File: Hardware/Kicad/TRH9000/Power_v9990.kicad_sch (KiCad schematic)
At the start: 21 parts, among them U1 V9990, U2 KM428C256, U3 KM428C256, U4 74VHC138, U6 LMH1980, U7 T.I_SN74AHCT32D

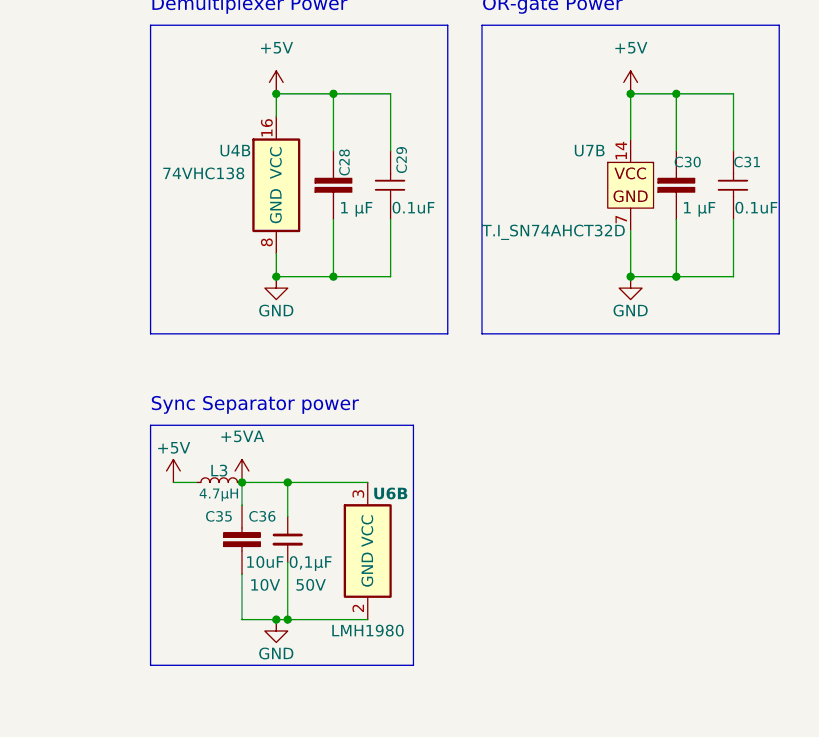
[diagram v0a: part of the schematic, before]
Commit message: Multiple updates. Routing. Almost finished routing for the VDP. Moved back the footprint for the 14mhz oscillator to THT as it is easier to find outside US/Europe and I have a bunch laying around here. Organized all components into the PCB. Removed the holed in the cartridge so I can better measure them in the standard MSX cartridge. Changed the RGB connector footprint to a shorter version so we can fit it in the standard size cartridge. Fixed multiple footprints to 0805 as we will be standardizing in that size.
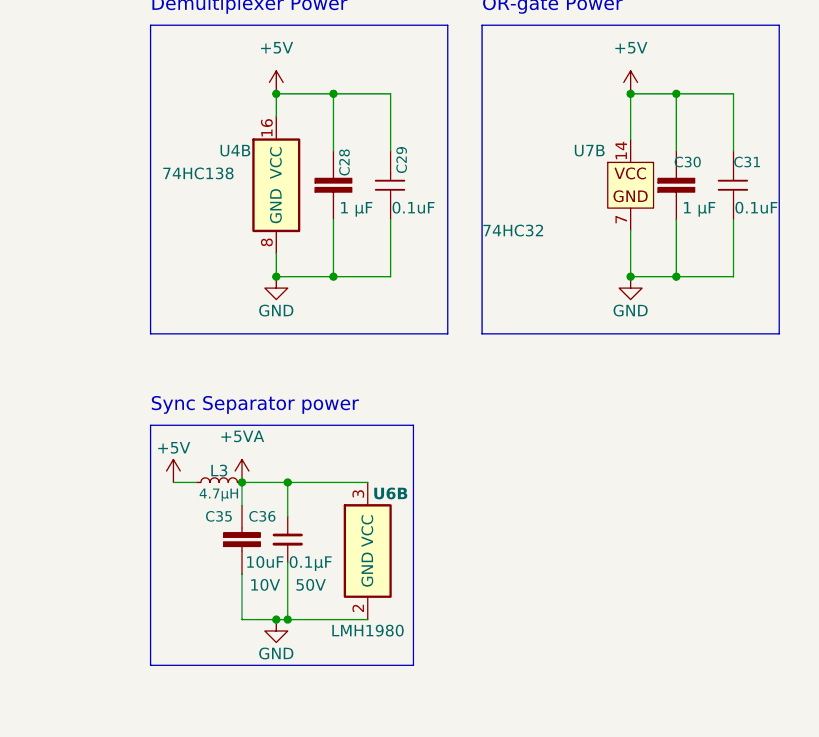
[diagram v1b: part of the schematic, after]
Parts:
- C28, C30: value C_CL21B105KBFNNNF -> 1 µF; footprint Capacitor_SMD:C_0805_2012Metric_Pad1.18x1.45mm_HandSolder -> Capacitor_SMD:C_0805_2012Metric
- C29: value C_CC0805JPX7R9BB104 -> 0.1uF; MPN CC0805JPX7R9BB104 -> (none); Manufacturer Yageo -> (none); Mounting type SMD -> (none); Mouser datasheet https://www.mouser.se/datasheet/2/427/vjcommercialseries-17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 -> (none); Price €0,14 -> (none); Status Active -> (none); Temperature Coefficient  X7R -> (none); Voltage rating 50V -> (none)
- C3: value C_GRM21BR61A476ME15K -> 47uF
- C31: value C_CC0805JPX7R9BB104 -> 0.1uF; MPN CC0805JPX7R9BB104 -> (none); Manufacturer Yageo -> (none); Mouser datasheet https://www.mouser.se/datasheet/2/427/vjcommercialseries-17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 -> (none)
- C35: value C_GRM21BR71A106KA73K -> 10uF
- C36: value C_CL10B104KB8NNNL -> 0.1µF; footprint Capacitor_SMD:C_0603_1608Metric_Pad1.08x0.95mm_HandSolder -> Capacitor_SMD:C_0805_2012Metric; Capacitance  0,1µF -> 0.1µF
- C5, C7: value C_CC0805JPX7R9BB104 -> 0.1uF
- L3: value L_MLZ2012M4R7HT000 -> 4.7µH
- U4: value 74VHC138 -> 74HC138; MPN 74VHC138FT -> 74HC138
- U7: value T.I_SN74AHCT32D -> 74HC32; footprint trh9000:Texas_R-PDSO-G14_3.6x4.4mm -> Package_SO:SO-14_3.9x8.65mm_P1.27mm; MPN SN74AHCT32DGVR -> 74HC32
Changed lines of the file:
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@@
       (effects (font (size 1.143 1.143)) (justify left))
     )
-    (property "Value" "C_CC0805JPX7R9BB104" (id 1) (at 193.04 53.34 0)
+    (property "Value" "0.1uF" (id 1) (at 193.04 53.34 0)
       (effects (font (size 1.143 1.143)) (justify left bottom) hide)
     )
@@
       (effects (font (size 1.143 1.143)))
     )
-    (property "Value" "C_CL21B105KBFNNNF" (id 1) (at 62.484 46.609 0)
+    (property "Value" "1 µF" (id 1) (at 62.484 46.609 0)
       (effects (font (size 1.143 1.143)) (justify left bottom) hide)
     )
-    (property "Footprint" "Capacitor_SMD:C_0805_2012Metric_Pad1.18x1.45mm_HandSolder" (id 2) (at 60.96 52.07 0)
+    (property "Footprint" "Capacitor_SMD:C_0805_2012Metric" (id 2) (at 60.96 52.07 0)
       (effects (font (size 0.508 0.508)) hide)
     )
@@
       (effects (font (size 1.143 1.143)) (justify left))
     )
-    (property "Value" "C_CL10B104KB8NNNL" (id 1) (at 55.626 84.582 0)
+    (property "Value" " 0.1µF" (id 1) (at 55.626 84.582 0)
       (effects (font (size 1.27 1.27)) (justify left) hide)
     )
-    (property "Footprint" "Capacitor_SMD:C_0603_1608Metric_Pad1.08x0.95mm_HandSolder" (id 2) (at 2.54 91.44 0)
+    (property "Footprint" "Capacitor_SMD:C_0805_2012Metric" (id 2) (at 2.54 91.44 0)
       (effects (font (size 1.27 1.27)) hide)
     )
@@
       (effects (font (size 2.54 2.54)) hide)
     )
-    (property "Capacitance " " 0,1µF" (id 7) (at 58.42 85.09 0))
+    (property "Capacitance " " 0.1µF" (id 7) (at 58.42 85.09 0))
     (property "Tolerance" " ±10% " (id 8) (at 29.21 72.39 0)
       (effects (font (size 2.54 2.54)) hide)
@@
       (effects (font (size 1.27 1.27)) (justify left))
     )
-    (property "Value" "74VHC138" (id 1) (at 41.91 41.91 0)
+    (property "Value" "74HC138" (id 1) (at 41.91 41.91 0)
       (effects (font (size 1.27 1.27)) (justify left))
     )
@@
       (effects (font (size 1.27 1.27)) hide)
     )
-    (property "MPN" "74VHC138FT" (id 4) (at 80.01 45.72 0)
+    (property "MPN" "74HC138" (id 4) (at 80.01 45.72 0)
       (effects (font (size 1.27 1.27)) hide)
     )
@@
       (effects (font (size 1.143 1.143)) (justify left))
     )
-    (property "Value" "C_CC0805JPX7R9BB104" (id 1) (at 214.63 53.34 0)
+    (property "Value" "0.1uF" (id 1) (at 214.63 53.34 0)
       (effects (font (size 1.143 1.143)) (justify left bottom) hide)
     )
@@
     (in_bom yes) (on_board yes)
     (property "Reference" "L3" (id 0) (at 48.26 74.93 90))
-    (property "Value" "L_MLZ2012M4R7HT000" (id 1) (at 49.276 75.438 0)
+    (property "Value" "4.7µH" (id 1) (at 49.276 75.438 0)
       (effects (font (size 1.27 1.27)) (justify left) hide)
     )
@@
       (effects (font (size 1.143 1.143)) (justify left))
     )
-    (property "Value" "C_GRM21BR61A476ME15K" (id 1) (at 161.29 73.66 0)
+    (property "Value" "47uF" (id 1) (at 161.29 73.66 0)
       (effects (font (size 1.143 1.143)) (justify left) hide)
     )
@@
       (effects (font (size 1.143 1.143)) (justify left))
     )
-    (property "Value" "C_CC0805JPX7R9BB104" (id 1) (at 72.39 49.53 0)
+    (property "Value" "0.1uF" (id 1) (at 72.39 49.53 0)
       (effects (font (size 1.143 1.143)) (justify left bottom) hide)
     )
@@
       (effects (font (size 0.508 0.508)) hide)
     )
-    (property "Datasheet" "https://www.yageo.com/upload/media/product/productsearch/datasheet/mlcc/UPY-GPHC_X7R_6.3V-to-50V_18.pdf" (id 3) (at 67.31 44.45 0)
-      (effects (font (size 1.27 1.27)) hide)
-    )
-    (property "Manufacturer" "Yageo" (id 4) (at 76.2 39.37 0)
-      (effects (font (size 1.27 1.27)) hide)
-    )
-    (property "MPN" "CC0805JPX7R9BB104" (id 5) (at 69.85 44.4499 0)
-      (effects (font (size 1.27 1.27)) (justify left) hide)
-    )
-    (property "Mouser datasheet" "https://www.mouser.se/datasheet/2/427/vjcommercialseries-1764145.pdf" (id 6) (at 109.22 41.91 0)
+    (property "Datasheet" "" (id 3) (at 67.31 44.45 0)
       (effects (font (size 1.27 1.27)) hide)
     )
     (property "Capacitance" "0.1uF" (id 7) (at 69.85 45.72 0))
-    (property "Voltage rating" "50V" (id 8) (at 74.93 46.99 0)
-      (effects (font (size 1.27 1.27)) hide)
-    )
-    (property "Temperature Coefficient " "X7R" (id 9) (at 74.93 52.07 0)
-      (effects (font (size 1.27 1.27)) hide)
-    )
-    (property "Mounting type" "SMD" (id 10) (at 76.2 59.69 0)
-      (effects (font (size 1.27 1.27)) hide)
-    )
-    (property "Status" "Active" (id 11) (at 76.2 54.61 0)
-      (effects (font (size 1.27 1.27)) hide)
-    )
-    (property "Price" "€0,14" (id 12) (at 76.2 57.15 0)
-      (effects (font (size 1.27 1.27)) hide)
-    )
     (pin "1")
     (pin "2")
@@
       (effects (font (size 1.143 1.143)))
     )
-    (property "Value" "C_CL21B105KBFNNNF" (id 1) (at 100.584 46.609 0)
+    (property "Value" "1 µF" (id 1) (at 100.584 46.609 0)
       (effects (font (size 1.143 1.143)) (justify left bottom) hide)
     )
-    (property "Footprint" "Capacitor_SMD:C_0805_2012Metric_Pad1.18x1.45mm_HandSolder" (id 2) (at 99.06 52.07 0)
+    (property "Footprint" "Capacitor_SMD:C_0805_2012Metric" (id 2) (at 99.06 52.07 0)
       (effects (font (size 0.508 0.508)) hide)
     )
@@
       (effects (font (size 1.143 1.143)) (justify left))
     )
-    (property "Value" "C_CC0805JPX7R9BB104" (id 1) (at 110.49 49.53 0)
+    (property "Value" "0.1uF" (id 1) (at 110.49 49.53 0)
       (effects (font (size 1.143 1.143)) (justify left bottom) hide)
     )
@@
     )
     (property "Datasheet" "https://www.yageo.com/upload/media/product/productsearch/datasheet/mlcc/UPY-GPHC_X7R_6.3V-to-50V_18.pdf" (id 3) (at 105.41 44.45 0)
-      (effects (font (size 1.27 1.27)) hide)
-    )
-    (property "Manufacturer" "Yageo" (id 4) (at 114.3 39.37 0)
-      (effects (font (size 1.27 1.27)) hide)
-    )
-    (property "MPN" "CC0805JPX7R9BB104" (id 5) (at 107.95 44.4499 0)
-      (effects (font (size 1.27 1.27)) (justify left) hide)
-    )
-    (property "Mouser datasheet" "https://www.mouser.se/datasheet/2/427/vjcommercialseries-1764145.pdf" (id 6) (at 147.32 41.91 0)
       (effects (font (size 1.27 1.27)) hide)
     )
@@
       (effects (font (size 1.143 1.143)))
     )
-    (property "Value" "C_GRM21BR71A106KA73K" (id 1) (at 52.07 85.09 0)
+    (property "Value" "10uF" (id 1) (at 52.07 85.09 0)
       (effects (font (size 1.143 1.143)) (justify left bottom) hide)
     )
@@
       (effects (font (size 1.27 1.27)) (justify left))
     )
-    (property "Value" "T.I_SN74AHCT32D" (id 1) (at 77.47 48.26 0)
-      (effects (font (size 1.27 1.27)) (justify left))
-    )
-    (property "Footprint" "trh9000:Texas_R-PDSO-G14_3.6x4.4mm" (id 2) (at 106.68 40.64 0)
+    (property "Value" "74HC32" (id 1) (at 77.47 48.26 0)
+      (effects (font (size 1.27 1.27)) (justify left))
+    )
+    (property "Footprint" "Package_SO:SO-14_3.9x8.65mm_P1.27mm" (id 2) (at 106.68 40.64 0)
       (effects (font (size 1.524 1.524)) (justify left) hide)
     )
@@
       (effects (font (size 1.524 1.524)) (justify left) hide)
     )
-    (property "MPN" "SN74AHCT32DGVR" (id 5) (at 106.68 33.02 0)
+    (property "MPN" "74HC32" (id 5) (at 106.68 33.02 0)
       (effects (font (size 1.524 1.524)) (justify left) hide)
     )

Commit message: Routing, readme, etc
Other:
- moved on the sheet: U1D
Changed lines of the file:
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@@
     (stroke (width 0) (type default) (color 0 0 0 0))
   )
-  (wire (pts (xy 125.73 48.26) (xy 128.27 48.26))
+  (wire (pts (xy 133.35 48.26) (xy 135.89 48.26))
     (stroke (width 0) (type default) (color 0 0 0 0))
   )
@@
     (stroke (width 0) (type default) (color 0 0 0 0))
   )
-  (wire (pts (xy 133.35 48.26) (xy 135.89 48.26))
+  (wire (pts (xy 140.97 48.26) (xy 143.51 48.26))
     (stroke (width 0) (type default) (color 0 0 0 0))
   )
@@
     (stroke (width 0) (type default) (color 0 0 0 0))
   )
+  (wire (pts (xy 140.97 33.02) (xy 143.51 33.02))
+    (stroke (width 0) (type default) (color 0 0 0 0))
+  )
+  (wire (pts (xy 157.48 68.58) (xy 171.45 68.58))
+    (stroke (width 0) (type default) (color 0 0 0 0))
+  )
+  (wire (pts (xy 170.18 39.37) (xy 167.64 39.37))
+    (stroke (width 0) (type default) (color 0 0 0 0))
+  )
+  (polyline (pts (xy 40.64 25.4) (xy 40.64 59.69))
+    (stroke (width 0) (type default) (color 0 0 0 0))
+  )
+  (polyline (pts (xy 115.57 25.4) (xy 115.57 90.17))
+    (stroke (width 0) (type default) (color 0 0 0 0))
+  )
+  (wire (pts (xy 105.41 33.02) (xy 99.06 33.02))
+    (stroke (width 0) (type default) (color 0 0 0 0))
+  )
   (wire (pts (xy 133.35 33.02) (xy 135.89 33.02))
-    (stroke (width 0) (type default) (color 0 0 0 0))
-  )
-  (wire (pts (xy 157.48 68.58) (xy 171.45 68.58))
-    (stroke (width 0) (type default) (color 0 0 0 0))
-  )
-  (wire (pts (xy 170.18 39.37) (xy 167.64 39.37))
-    (stroke (width 0) (type default) (color 0 0 0 0))
-  )
-  (polyline (pts (xy 40.64 25.4) (xy 40.64 59.69))
-    (stroke (width 0) (type default) (color 0 0 0 0))
-  )
-  (polyline (pts (xy 115.57 25.4) (xy 115.57 90.17))
-    (stroke (width 0) (type default) (color 0 0 0 0))
-  )
-  (wire (pts (xy 105.41 33.02) (xy 99.06 33.02))
-    (stroke (width 0) (type default) (color 0 0 0 0))
-  )
-  (wire (pts (xy 125.73 33.02) (xy 128.27 33.02))
     (stroke (width 0) (type default) (color 0 0 0 0))
   )
@@
     (pin "2")
   )
-  (symbol (lib_id "power:+5VA") (at 135.89 33.02 0) (unit 1)
-    (in_bom yes) (on_board yes)
-    (property "Reference" "#PWR0109" (id 0) (at 135.89 36.83 0)
-      (effects (font (size 1.27 1.27)) hide)
-    )
-    (property "Value" "+5VA" (id 1) (at 136.271 28.6258 0))
-    (property "Footprint" "" (id 2) (at 135.89 33.02 0)
-      (effects (font (size 1.27 1.27)) hide)
-    )
-    (property "Datasheet" "" (id 3) (at 135.89 33.02 0)
+  (symbol (lib_id "power:+5VA") (at 143.51 33.02 0) (unit 1)
+    (in_bom yes) (on_board yes)
+    (property "Reference" "#PWR0109" (id 0) (at 143.51 36.83 0)
+      (effects (font (size 1.27 1.27)) hide)
+    )
+    (property "Value" "+5VA" (id 1) (at 143.891 28.6258 0))
+    (property "Footprint" "" (id 2) (at 143.51 33.02 0)
+      (effects (font (size 1.27 1.27)) hide)
+    )
+    (property "Datasheet" "" (id 3) (at 143.51 33.02 0)
       (effects (font (size 1.27 1.27)) hide)
     )
@@
     (pin "1")
   )
-  (symbol (lib_id "power:GND") (at 125.73 48.26 0) (unit 1)
-    (in_bom yes) (on_board yes)
-    (property "Reference" "#PWR0123" (id 0) (at 125.73 54.61 0)
-      (effects (font (size 1.27 1.27)) hide)
-    )
-    (property "Value" "GND" (id 1) (at 125.857 52.6542 0))
-    (property "Footprint" "" (id 2) (at 125.73 48.26 0)
-      (effects (font (size 1.27 1.27)) hide)
-    )
-    (property "Datasheet" "" (id 3) (at 125.73 48.26 0)
+  (symbol (lib_id "power:GND") (at 133.35 48.26 0) (unit 1)
+    (in_bom yes) (on_board yes)
+    (property "Reference" "#PWR0123" (id 0) (at 133.35 54.61 0)
+      (effects (font (size 1.27 1.27)) hide)
+    )
+    (property "Value" "GND" (id 1) (at 133.477 52.6542 0))
+    (property "Footprint" "" (id 2) (at 133.35 48.26 0)
+      (effects (font (size 1.27 1.27)) hide)
+    )
+    (property "Datasheet" "" (id 3) (at 133.35 48.26 0)
       (effects (font (size 1.27 1.27)) hide)
     )
@@
     (pin "1")
   )
-  (symbol (lib_id "TRH9000:V9990") (at 130.81 40.64 0) (unit 4)
-    (in_bom yes) (on_board yes)
-    (property "Reference" "U1" (id 0) (at 121.92 36.83 0)
+  (symbol (lib_id "TRH9000:V9990") (at 138.43 40.64 0) (unit 4)
+    (in_bom yes) (on_board yes)
+    (property "Reference" "U1" (id 0) (at 129.54 36.83 0)
       (effects (font (size 1.27 1.27)) (justify left))
     )
-    (property "Value" "V9990" (id 1) (at 121.92 44.45 0)
+    (property "Value" "V9990" (id 1) (at 129.54 44.45 0)
       (effects (font (size 1.524 1.524)) (justify left))
     )
-    (property "Footprint" "trh9000:LQFP-128_28x28mm_P0.8mm" (id 2) (at 130.81 40.64 0)
+    (property "Footprint" "trh9000:LQFP-128_28x28mm_P0.8mm" (id 2) (at 138.43 40.64 0)
       (effects (font (size 1.524 1.524)) hide)
     )
-    (property "Datasheet" "https://www.msx.org/wiki/Yamaha_V9990" (id 3) (at 130.81 40.64 0)
+    (property "Datasheet" "https://www.msx.org/wiki/Yamaha_V9990" (id 3) (at 138.43 40.64 0)
       (effects (font (size 1.524 1.524)) hide)
     )
-    (property "Manufacturer" "Yamaha" (id 4) (at 67.31 -7.62 0)
+    (property "Manufacturer" "Yamaha" (id 4) (at 74.93 -7.62 0)
       (effects (font (size 1.524 1.524)) hide)
     )
-    (property "MPN" "V9990" (id 5) (at 67.31 0 0)
+    (property "MPN" "V9990" (id 5) (at 74.93 0 0)
       (effects (font (size 1.524 1.524)) hide)
     )
-    (property "Description" "Video Display Processor (VDP)" (id 6) (at 80.01 -5.08 0)
+    (property "Description" "Video Display Processor (VDP)" (id 6) (at 87.63 -5.08 0)
       (effects (font (size 1.524 1.524)) hide)
     )
@@
     (pin "96")
   )
-  (symbol (lib_id "power:GNDA") (at 135.89 48.26 0) (unit 1)
-    (in_bom yes) (on_board yes)
-    (property "Reference" "#PWR0128" (id 0) (at 135.89 54.61 0)
-      (effects (font (size 1.27 1.27)) hide)
-    )
-    (property "Value" "GNDA" (id 1) (at 136.017 52.6542 0))
-    (property "Footprint" "" (id 2) (at 135.89 48.26 0)
-      (effects (font (size 1.27 1.27)) hide)
-    )
-    (property "Datasheet" "" (id 3) (at 135.89 48.26 0)
+  (symbol (lib_id "power:GNDA") (at 143.51 48.26 0) (unit 1)
+    (in_bom yes) (on_board yes)
+    (property "Reference" "#PWR0128" (id 0) (at 143.51 54.61 0)
+      (effects (font (size 1.27 1.27)) hide)
+    )
+    (property "Value" "GNDA" (id 1) (at 143.637 52.6542 0))
+    (property "Footprint" "" (id 2) (at 143.51 48.26 0)
+      (effects (font (size 1.27 1.27)) hide)
+    )
+    (property "Datasheet" "" (id 3) (at 143.51 48.26 0)
       (effects (font (size 1.27 1.27)) hide)
     )
@@
     (pin "40")
   )
-  (symbol (lib_id "power:+5V") (at 125.73 33.02 0) (unit 1)
-    (in_bom yes) (on_board yes)
-    (property "Reference" "#PWR0110" (id 0) (at 125.73 36.83 0)
-      (effects (font (size 1.27 1.27)) hide)
-    )
-    (property "Value" "+5V" (id 1) (at 126.111 28.6258 0))
-    (property "Footprint" "" (id 2) (at 125.73 33.02 0)
-      (effects (font (size 1.27 1.27)) hide)
-    )
-    (property "Datasheet" "" (id 3) (at 125.73 33.02 0)
-      (effects (font (size 1.27 1.27)) hide)
-    )
+  (symbol (lib_id "power:+5V") (at 133.35 33.02 0) (unit 1)
+    (in_bom yes) (on_board yes)
+    (property "Reference" "#PWR0110" (id 0) (at 133.35 36.83 0)
+      (effects (font (size 1.27 1.27)) hide)
+    )
+    (property "Value" "+5V" (id 1) (at 133.731 28.6258 0))
+    (property "Footprint" "" (id 2) (at 133.35 33.02 0)
+      (effects (font (size 1.27 1.27)) hide)
+    )
+    (property "Datasheet" "" (id 3) (at 133.35 33.02 0)
+      (effects (font (size 1.27 1.27)) hide)
+    )
